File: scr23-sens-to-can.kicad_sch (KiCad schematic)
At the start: 63 parts, among them IC1 ADS1256IDBRG4, J1 ATM13-12PA-BM01, J2 6473711-1, J3 Conn_ST_STDC14, SW1 SW_SPDT, U1 SRV05-4, U10 AP63205WU, U2 SRV05-4, U3 LM4040DCK-2.5, U4 TJA1042T-3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

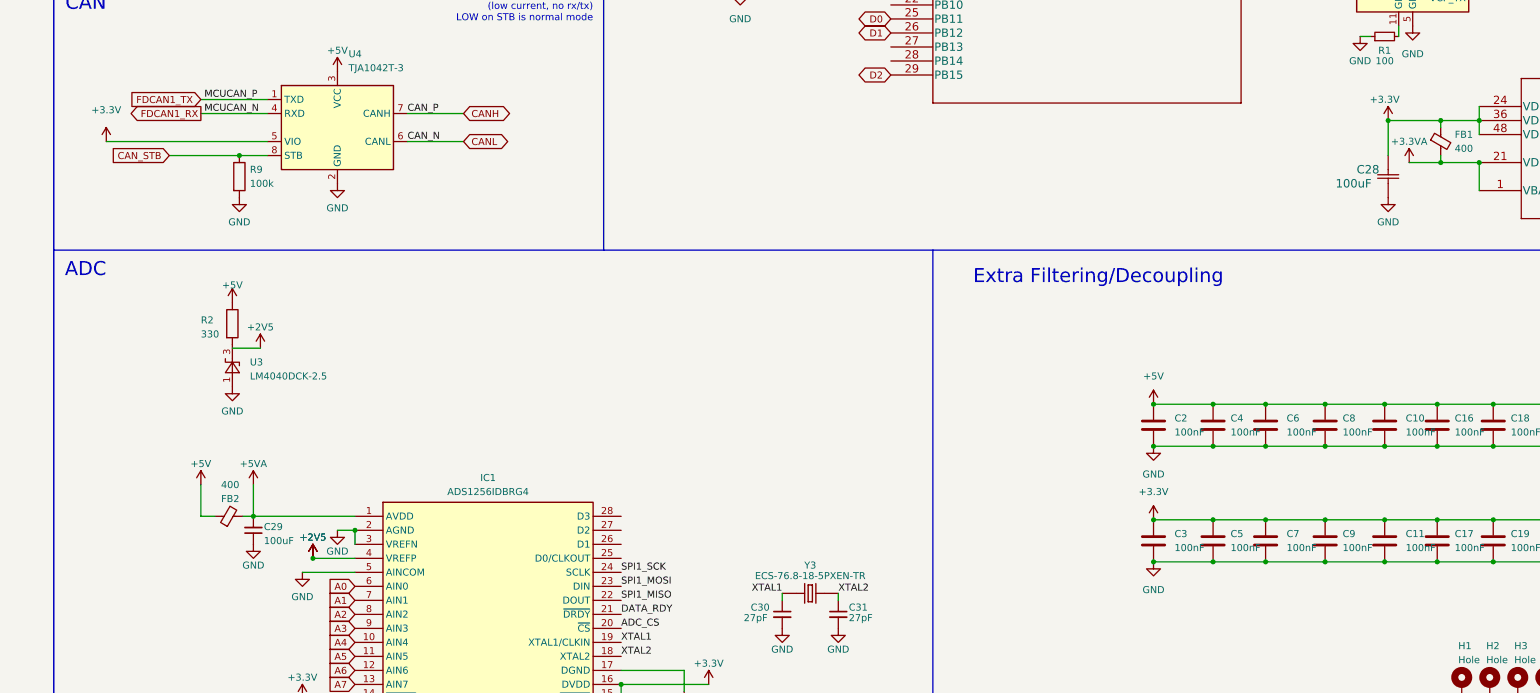
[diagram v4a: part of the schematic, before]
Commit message: add tantalum 10u cap and 0R resistor to tune ferrite bead filter
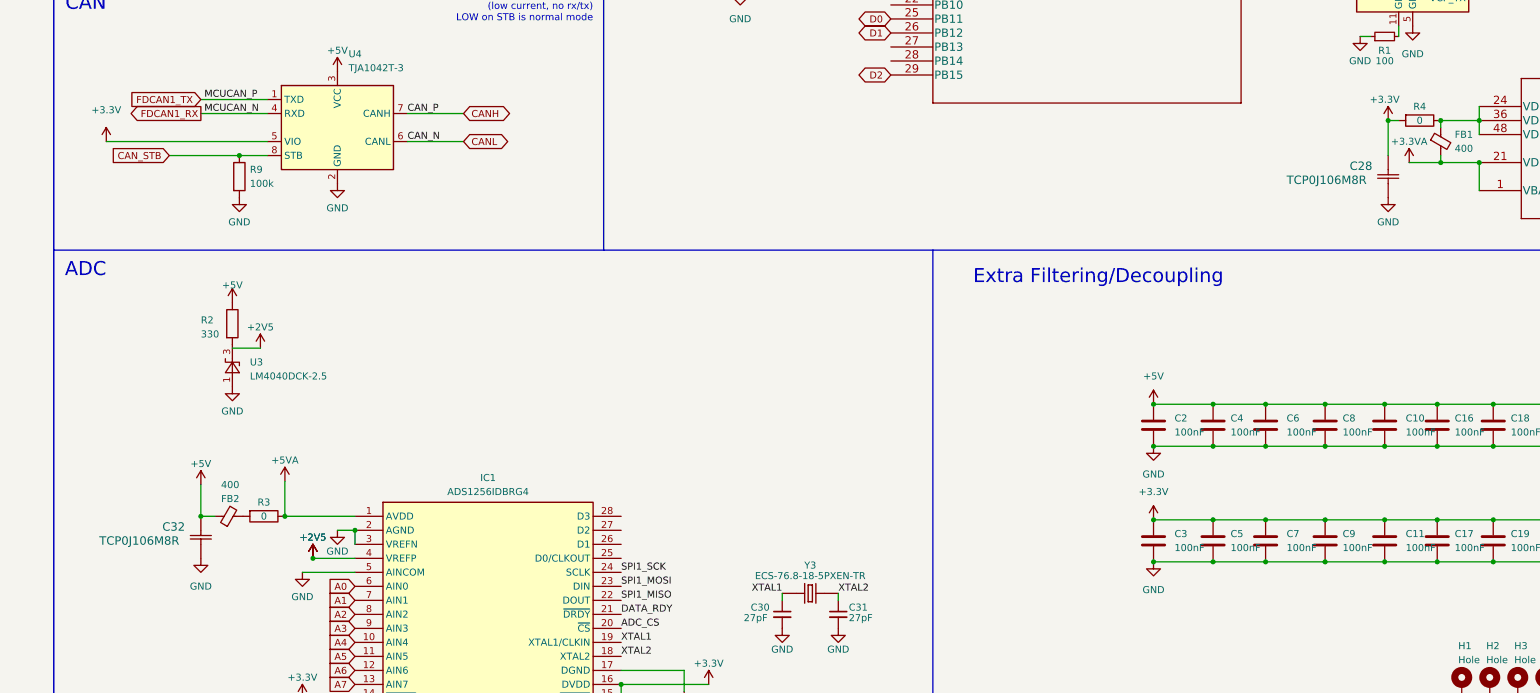
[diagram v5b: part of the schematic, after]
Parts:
- removed C29: 100uF, Capacitor_SMD:C_0805_2012Metric, symbol Device:C_Small
- added C32: TCP0J106M8R, Capacitor_SMD:C_0805_2012Metric, symbol scr23-sens-to-can-main:TCJA107M004R0200
- added R3, R4: 0, Resistor_SMD:R_0603_1608Metric_Pad0.98x0.95mm_HandSolder, symbol Device:R
- C28: value 100uF -> TCP0J106M8R
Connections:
- net +3.3V: now also R4.2; no longer FB1.1, U8.24 (VDD), U8.36 (VDD), U8.48 (VDD)
- net +5V: now also C32.1
- net +5VA: now also R3.1; no longer FB2.2
- net GND: now also C32.2
- new net: FB1.1, R4.1, U8.24 (VDD), U8.36 (VDD), U8.48 (VDD)
- new net: FB2.2, R3.2
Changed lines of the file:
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@@
   (junction (at 174.625 69.85) (diameter 0) (color 0 0 0 0)
   )
+  (junction (at 352.425 123.825) (diameter 0) (color 0 0 0 0)
+  )
   (junction (at 340.995 182.88) (diameter 0) (color 0 0 0 0)
   )
@@
   (junction (at 31.75 210.185) (diameter 0) (color 0 0 0 0)
   )
-  (junction (at 352.425 123.825) (diameter 0) (color 0 0 0 0)
-  )
   (junction (at 368.935 131.445) (diameter 0) (color 0 0 0 0)
   )
@@
   (junction (at 368.935 123.825) (diameter 0) (color 0 0 0 0)
   )
+  (junction (at 137.16 195.58) (diameter 0) (color 0 0 0 0)
+  )
   (junction (at 351.79 182.88) (diameter 0) (color 0 0 0 0)
   )
@@
   (junction (at 351.79 175.26) (diameter 0) (color 0 0 0 0)
   )
-  (junction (at 146.685 195.58) (diameter 0) (color 0 0 0 0)
-  )
-  (junction (at 361.95 123.825) (diameter 0) (color 0 0 0 0)
-  )
   (junction (at 330.2 203.835) (diameter 0) (color 0 0 0 0)
   )
   (junction (at 174.625 46.99) (diameter 0) (color 0 0 0 0)
   )
+  (junction (at 361.95 123.825) (diameter 0) (color 0 0 0 0)
+  )
   (junction (at 320.675 203.835) (diameter 0) (color 0 0 0 0)
   )
@@
   (junction (at 365.76 228.6) (diameter 0) (color 0 0 0 0)
   )
+  (junction (at 152.4 195.58) (diameter 0) (color 0 0 0 0)
+  )
   (junction (at 31.75 184.785) (diameter 0) (color 0 0 0 0)
   )
@@
     (stroke (width 0) (type default))
   )
-  (wire (pts (xy 144.78 195.58) (xy 146.685 195.58))
-    (stroke (width 0) (type default))
-  )
   (wire (pts (xy 31.75 215.265) (xy 31.75 217.805))
     (stroke (width 0) (type default))
@@
     (stroke (width 0) (type default))
   )
+  (wire (pts (xy 152.4 195.58) (xy 165.1 195.58))
+    (stroke (width 0) (type default))
+  )
   (wire (pts (xy 247.015 97.79) (xy 262.255 97.79))
     (stroke (width 0) (type default))
@@
     (stroke (width 0) (type default))
   )
-  (wire (pts (xy 146.685 189.865) (xy 146.685 195.58))
+  (wire (pts (xy 152.4 189.23) (xy 152.4 195.58))
     (stroke (width 0) (type default))
   )
@@
     (stroke (width 0) (type default))
   )
-  (wire (pts (xy 352.425 123.825) (xy 361.95 123.825))
-    (stroke (width 0) (type default))
-  )
   (wire (pts (xy 320.675 175.26) (xy 330.2 175.26))
     (stroke (width 0) (type default))
@@
     (stroke (width 0) (type default))
   )
+  (wire (pts (xy 352.425 123.825) (xy 354.33 123.825))
+    (stroke (width 0) (type default))
+  )
   (wire (pts (xy 320.675 182.88) (xy 330.2 182.88))
     (stroke (width 0) (type default))
@@
     (stroke (width 0) (type default))
   )
-  (wire (pts (xy 146.685 195.58) (xy 165.1 195.58))
-    (stroke (width 0) (type default))
-  )
   (wire (pts (xy 170.815 69.85) (xy 170.815 77.47))
     (stroke (width 0) (type default))
@@
     )
   )
+  (symbol (lib_id "Device:R") (at 358.14 123.825 270) (unit 1)
+    (in_bom yes) (on_board yes) (dnp no)
+    (property "Reference" "R4" (at 358.14 121.285 90)
+      (effects (font (size 1.27 1.27)))
+    )
+    (property "Value" "0" (at 358.14 123.825 90)
+      (effects (font (size 1.27 1.27)))
+    )
+    (property "Footprint" "Resistor_SMD:R_0603_1608Metric_Pad0.98x0.95mm_HandSolder" (at 358.14 122.047 90)
+      (effects (font (size 1.27 1.27)) hide)
+    )
+    (property "Datasheet" "~" (at 358.14 123.825 0)
+      (effects (font (size 1.27 1.27)) hide)
+    )
+    (pin "1")
+    (pin "2")
+    (instances
+      (project "scr23-sens-to-can"
+        (path "/9d4a62b8-9a16-4c8d-8b16-7072bfb3ee3d"
+          (reference "R4") (unit 1)
+        )
+      )
+    )
+  )
   (symbol (lib_id "scr23-sens-to-can-main:AP7370-33Y-13") (at 153.67 39.37 0) (unit 1)
     (in_bom yes) (on_board yes) (dnp no) (fields_autoplaced)
@@
     )
   )
+  (symbol (lib_id "Device:R") (at 148.59 195.58 270) (unit 1)
+    (in_bom yes) (on_board yes) (dnp no)
+    (property "Reference" "R3" (at 148.59 193.04 90)
+      (effects (font (size 1.27 1.27)))
+    )
+    (property "Value" "0" (at 148.59 195.58 90)
+      (effects (font (size 1.27 1.27)))
+    )
+    (property "Footprint" "Resistor_SMD:R_0603_1608Metric_Pad0.98x0.95mm_HandSolder" (at 148.59 193.802 90)
+      (effects (font (size 1.27 1.27)) hide)
+    )
+    (property "Datasheet" "~" (at 148.59 195.58 0)
+      (effects (font (size 1.27 1.27)) hide)
+    )
+    (pin "1")
+    (pin "2")
+    (instances
+      (project "scr23-sens-to-can"
+        (path "/9d4a62b8-9a16-4c8d-8b16-7072bfb3ee3d"
+          (reference "R3") (unit 1)
+        )
+      )
+    )
+  )
   (symbol (lib_id "Switch:SW_SPDT") (at 241.935 97.79 0) (mirror y) (unit 1)
     (in_bom yes) (on_board yes) (dnp no) (fields_autoplaced)
@@
     )
   )
-  (symbol (lib_id "power:+5VA") (at 146.685 189.865 0) (unit 1)
+  (symbol (lib_id "power:+5VA") (at 152.4 189.23 0) (unit 1)
     (in_bom yes) (on_board yes) (dnp no)
-    (property "Reference" "#PWR017" (at 146.685 193.675 0)
+    (property "Reference" "#PWR017" (at 152.4 193.04 0)
       (effects (font (size 1.27 1.27)) hide)
     )
-    (property "Value" "+5VA" (at 146.685 186.055 0)
+    (property "Value" "+5VA" (at 152.4 185.42 0)
       (effects (font (size 1.27 1.27)))
     )
-    (property "Footprint" "" (at 146.685 189.865 0)
+    (property "Footprint" "" (at 152.4 189.23 0)
       (effects (font (size 1.27 1.27)) hide)
     )
-    (property "Datasheet" "" (at 146.685 189.865 0)
+    (property "Datasheet" "" (at 152.4 189.23 0)
       (effects (font (size 1.27 1.27)) hide)
     )
@@
   (symbol (lib_id "scr23-sens-to-can-main:TCJA107M004R0200") (at 352.425 130.175 270) (unit 1)
     (in_bom yes) (on_board yes) (dnp no)
-    (property "Reference" "C28" (at 346.71 132.715 90)
+    (property "Reference" "C28" (at 345.44 132.08 90)
       (effects (font (size 1.524 1.524)) (justify left))
     )
-    (property "Value" "100uF" (at 342.9 135.255 90)
+    (property "Value" "TCP0J106M8R" (at 334.01 134.62 90)
       (effects (font (size 1.524 1.524)) (justify left))
     )
@@
     )
   )
-  (symbol (lib_id "Device:C_Small") (at 146.685 198.12 180) (unit 1)
-    (in_bom yes) (on_board yes) (dnp no)
-    (property "Reference" "C29" (at 148.59 197.485 0)
-      (effects (font (size 1.27 1.27)) (justify right))
-    )
-    (property "Value" "100uF" (at 148.59 200.025 0)
-      (effects (font (size 1.27 1.27)) (justify right))
-    )
-    (property "Footprint" "Capacitor_SMD:C_0805_2012Metric" (at 146.685 198.12 0)
-      (effects (font (size 1.27 1.27)) hide)
-    )
-    (property "Datasheet" "~" (at 146.685 198.12 0)
-      (effects (font (size 1.27 1.27)) hide)
-    )
-    (pin "1")
-    (pin "2")
-    (instances
-      (project "scr23-sens-to-can"
-        (path "/9d4a62b8-9a16-4c8d-8b16-7072bfb3ee3d"
-          (reference "C29") (unit 1)
-        )
-      )
-    )
-  )
   (symbol (lib_id "Device:LED") (at 187.325 80.01 90) (unit 1)
     (in_bom yes) (on_board yes) (dnp no) (fields_autoplaced)
@@
     )
   )
-  (symbol (lib_id "power:GND") (at 146.685 200.66 0) (unit 1)
-    (in_bom yes) (on_board yes) (dnp no)
-    (property "Reference" "#PWR018" (at 146.685 207.01 0)
-      (effects (font (size 1.27 1.27)) hide)
-    )
-    (property "Value" "GND" (at 146.685 204.47 0)
-      (effects (font (size 1.27 1.27)))
-    )
-    (property "Footprint" "" (at 146.685 200.66 0)
-      (effects (font (size 1.27 1.27)) hide)
-    )
-    (property "Datasheet" "" (at 146.685 200.66 0)
-      (effects (font (size 1.27 1.27)) hide)
-    )
-    (pin "1")
-    (instances
-      (project "scr23-sens-to-can"
-        (path "/9d4a62b8-9a16-4c8d-8b16-7072bfb3ee3d"
-          (reference "#PWR018") (unit 1)
-        )
-      )
-    )
-  )
   (symbol (lib_id "Device:C") (at 351.79 179.07 180) (unit 1)
     (in_bom yes) (on_board yes) (dnp no) (fields_autoplaced)
@@
     )
   )
+  (symbol (lib_id "scr23-sens-to-can-main:TCJA107M004R0200") (at 137.16 195.58 270) (unit 1)
+    (in_bom yes) (on_board yes) (dnp no)
+    (property "Reference" "C32" (at 130.175 197.485 90)
+      (effects (font (size 1.524 1.524)) (justify left))
+    )
+    (property "Value" "TCP0J106M8R" (at 118.745 200.025 90)
+      (effects (font (size 1.524 1.524)) (justify left))
+    )
+    (property "Footprint" "Capacitor_SMD:C_0805_2012Metric" (at 128.016 199.39 0)
+      (effects (font (size 1.524 1.524)) hide)
+    )
+    (property "Datasheet" "https://datasheets.kyocera-avx.com/TCJ.pdf" (at 137.16 195.58 0)
+      (effects (font (size 1.524 1.524)) hide)
+    )
+    (pin "1")
+    (pin "2")
+    (instances
+      (project "scr23-sens-to-can"
+        (path "/9d4a62b8-9a16-4c8d-8b16-7072bfb3ee3d"
+          (reference "C32") (unit 1)
+        )
+      )
+    )
+  )
   (symbol (lib_id "Device:C") (at 382.27 179.07 180) (unit 1)
     (in_bom yes) (on_board yes) (dnp no) (fields_autoplaced)
@@
         )
       )
+    )
+  )
+  (symbol (lib_name "GND_7") (lib_id "power:GND") (at 137.16 203.2 0) (unit 1)
+    (in_bom yes) (on_board yes) (dnp no) (fields_autoplaced)
+    (property "Reference" "#PWR018" (at 137.16 209.55 0)
+      (effects (font (size 1.27 1.27)) hide)
+    )
+    (property "Value" "GND" (at 137.16 208.28 0)
+      (effects (font (size 1.27 1.27)))
+    )
+    (property "Footprint" "" (at 137.16 203.2 0)
+      (effects (font (size 1.27 1.27)) hide)
+    )
+    (property "Datasheet" "" (at 137.16 203.2 0)
+      (effects (font (size 1.27 1.27)) hide)
+    )
+    (pin "1")
+    (instances
+      (project "scr23-sens-to-can"
+        (path "/9d4a62b8-9a16-4c8d-8b16-7072bfb3ee3d"
+          (reference "#PWR018") (unit 1)
+        )
+      )

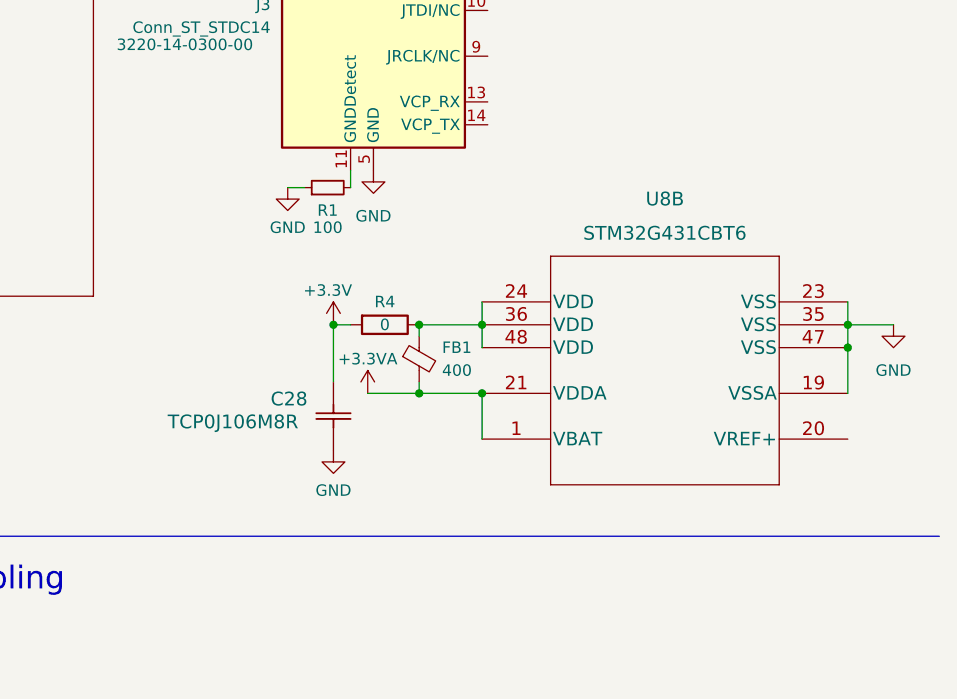
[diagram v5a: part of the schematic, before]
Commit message: add vref+ wiring to stm32g4
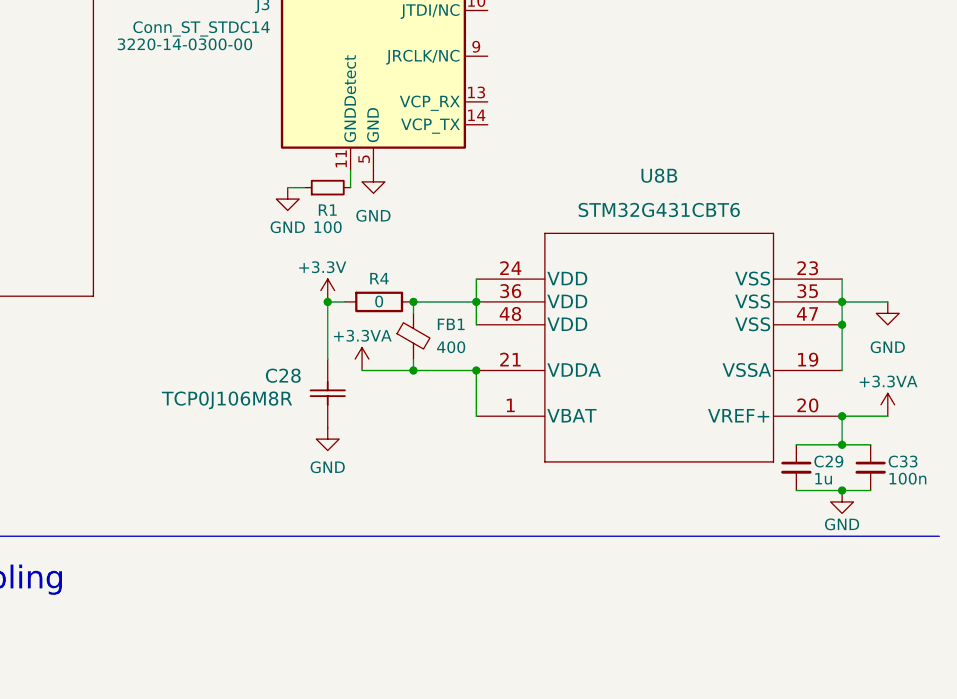
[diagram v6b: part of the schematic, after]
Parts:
- added C29: 1u, symbol Device:C_Small
- added C33: 100n, symbol Device:C_Small
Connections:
- net +3.3VA: now also U8.20 (VREF+), C29.1, C33.1
- net GND: now also C29.2, C33.2
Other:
- moved on the sheet: C28, FB1, R4, U8B

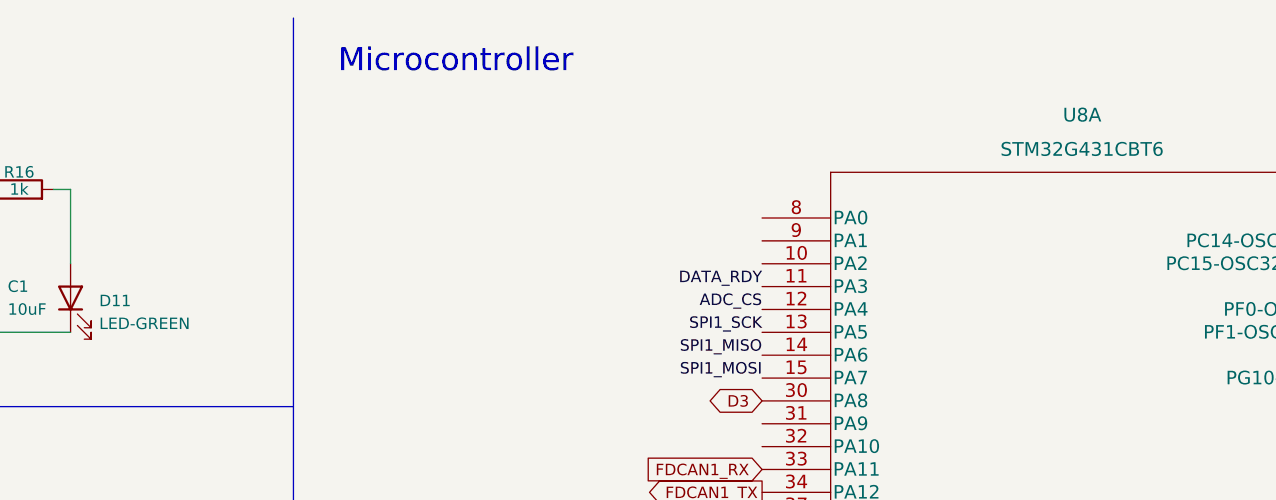
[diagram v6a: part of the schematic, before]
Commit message: switch voltage regulation scheme
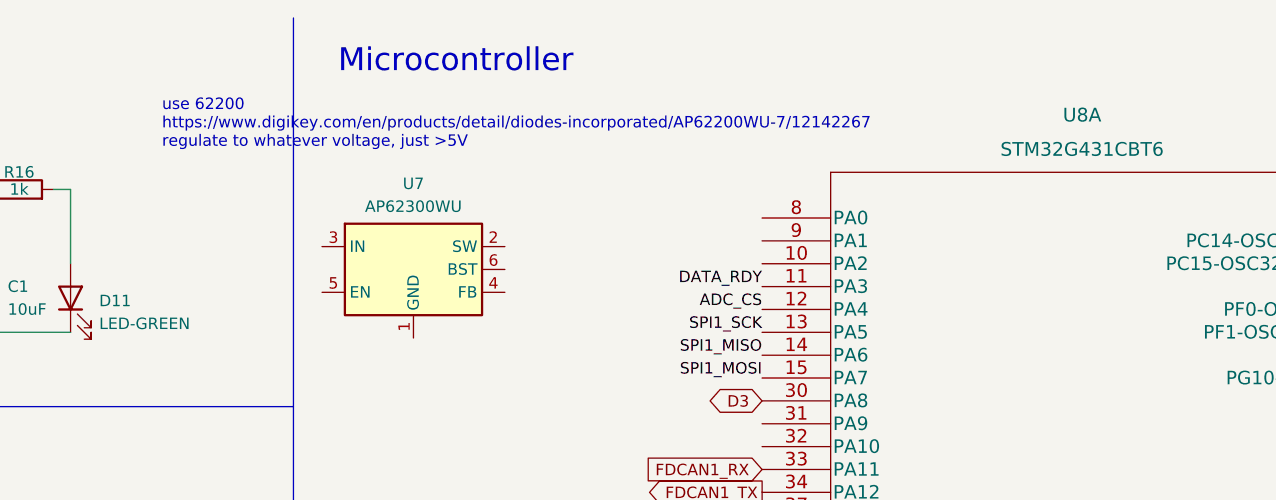
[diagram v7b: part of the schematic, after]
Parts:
- added U7: AP62300WU, Package_TO_SOT_SMD:TSOT-23-6, symbol Regulator_Switching:AP62300WU
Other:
- note added: "use 62200 https://www.digikey.com/en/products/detail/diodes-incorporated/AP62200WU-7/12142267 regulate to whatever voltage, just >5V"
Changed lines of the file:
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@@
     (effects (font (size 2.54 2.54)) (justify left bottom))
+  )
+  (text "use 62200\nhttps://www.digikey.com/en/products/detail/diodes-incorporated/AP62200WU-7/12142267\nregulate to whatever voltage, just >5V"
+    (at 195.58 26.67 0)
+    (effects (font (size 1.27 1.27)) (justify left bottom))
   )
   (text "CAN" (at 120.015 104.14 0)
@@
         )
       )
+    )
+  )
+  (symbol (lib_id "Regulator_Switching:AP62300WU") (at 223.52 40.005 0) (unit 1)
+    (in_bom yes) (on_board yes) (dnp no) (fields_autoplaced)
+    (property "Reference" "U7" (at 223.52 30.48 0)
+      (effects (font (size 1.27 1.27)))
+    )
+    (property "Value" "AP62300WU" (at 223.52 33.02 0)
+      (effects (font (size 1.27 1.27)))
+    )
+    (property "Footprint" "Package_TO_SOT_SMD:TSOT-23-6" (at 223.52 62.865 0)
+      (effects (font (size 1.27 1.27)) hide)
+    )
+    (property "Datasheet" "https://www.diodes.com/assets/Datasheets/AP62300_AP62301_AP62300T.pdf" (at 223.52 40.005 0)
+      (effects (font (size 1.27 1.27)) hide)
+    )
+    (pin "1")
+    (pin "2")
+    (pin "3")
+    (pin "4")
+    (pin "5")
+    (pin "6")
+    (instances
+      (project "scr23-sens-to-can"
+        (path "/9d4a62b8-9a16-4c8d-8b16-7072bfb3ee3d"
+          (reference "U7") (unit 1)
+        )
+      )
